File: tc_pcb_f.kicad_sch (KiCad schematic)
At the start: 7 parts, among them U1 32u4, U2 MAX31855, U3 MAX31855, U4 MAX31855, U5 MAX31855, U6 MAX31855, U7 extPWR

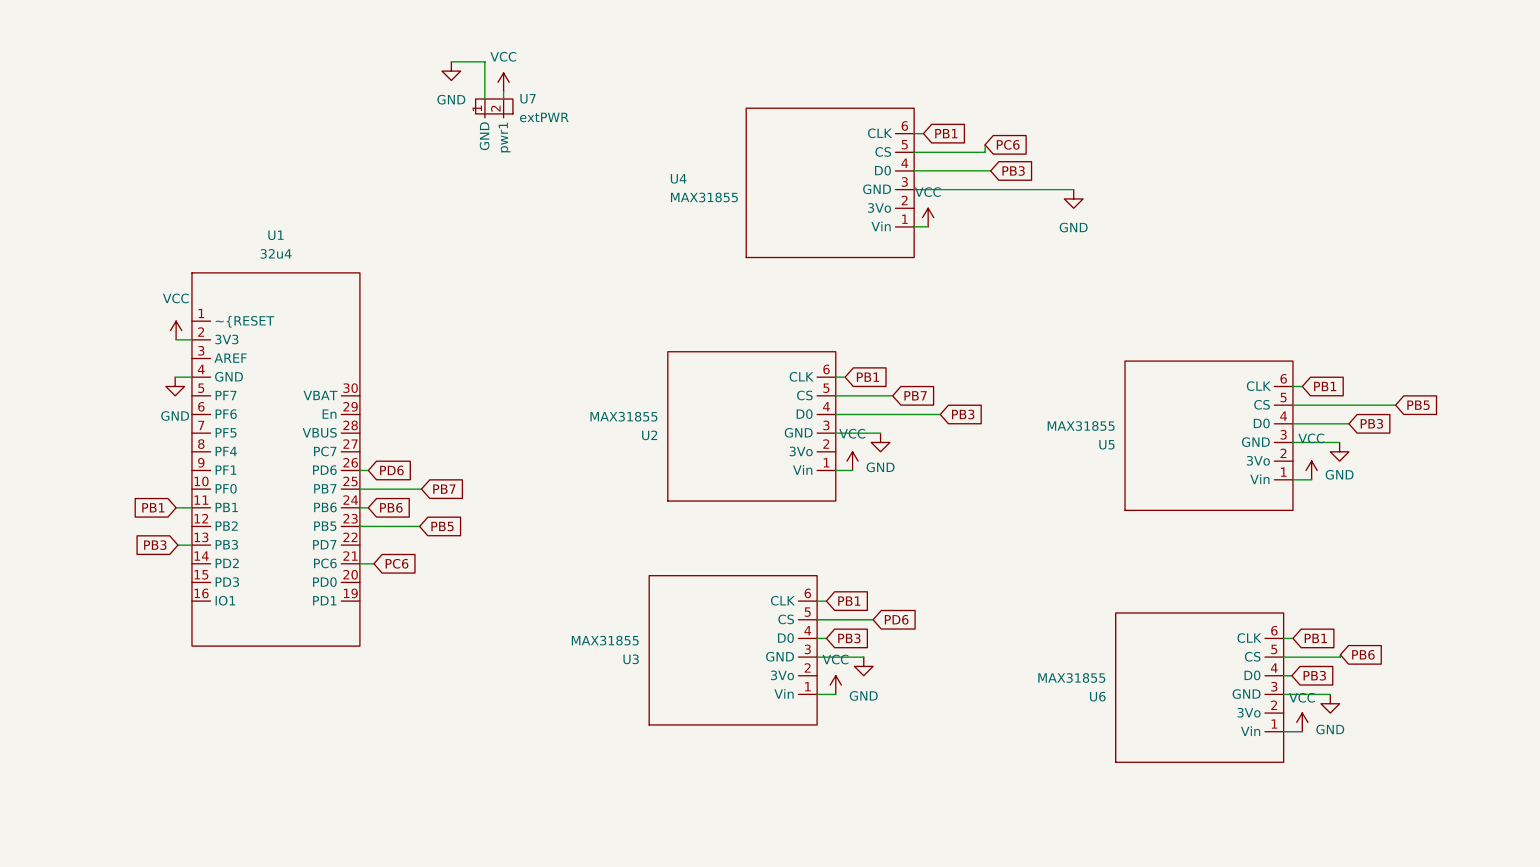
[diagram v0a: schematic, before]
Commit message: finished layout for 8 sensor board
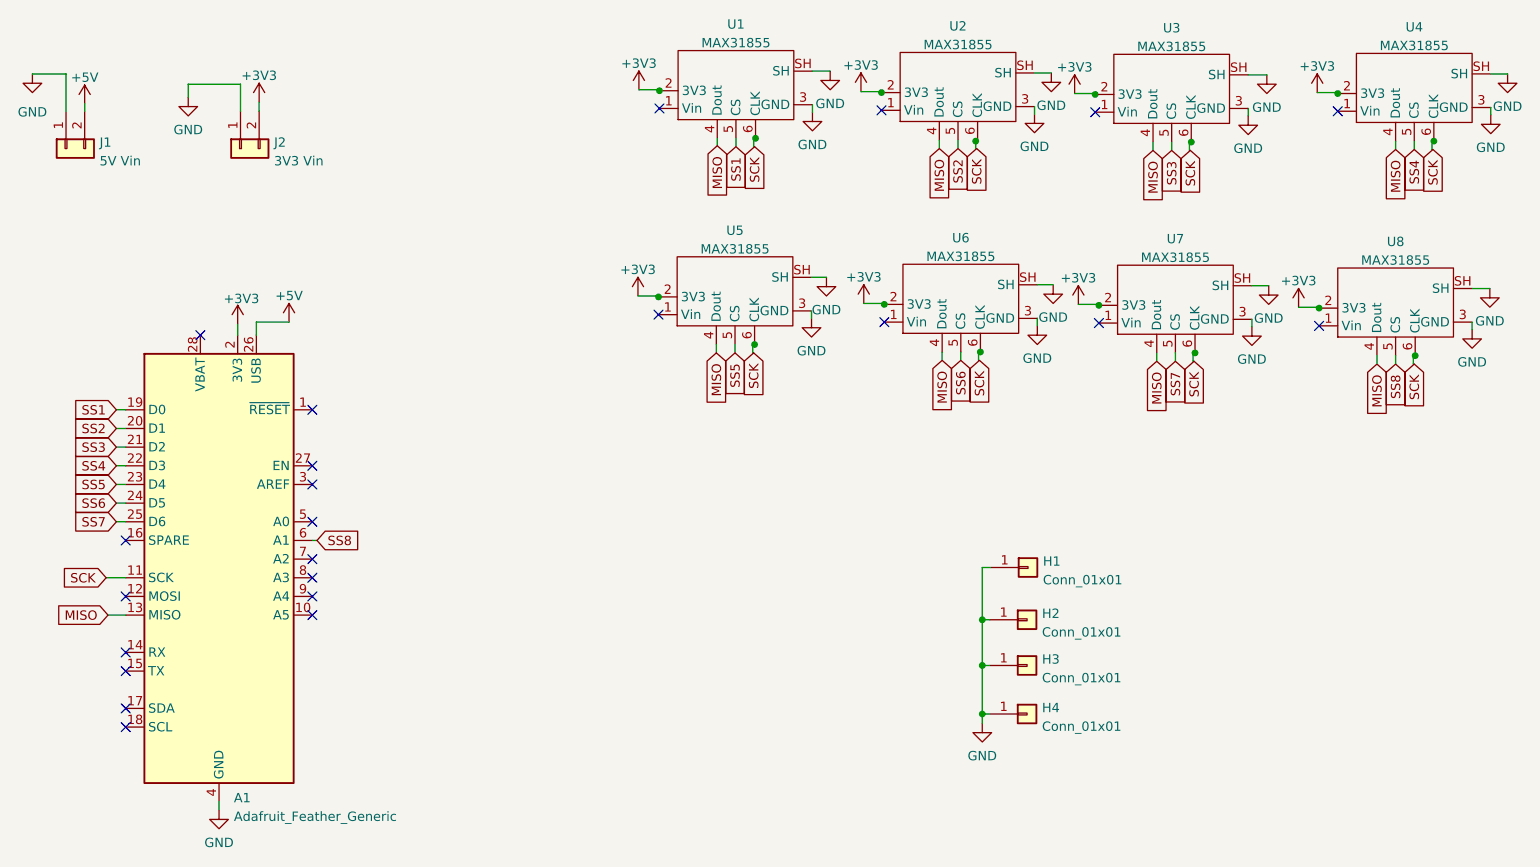
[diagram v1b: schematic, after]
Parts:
- removed U1: 32u4, thermo:32u4, symbol New_Library_0:32u4
- removed U2, U3, U4, U5, U6: MAX31855, thermo:MAX31855, symbol New_Library_0:MAX31855
- removed U7: extPWR, thermo:extPWR, symbol New_Library_0:extPWR
- added A1: Adafruit_Feather_Generic, mcu:Adafruit_Feather, symbol MCU_Module:Adafruit_Feather_Generic
- added H1, H2, H3, H4: Conn_01x01, mounting_holes:3mm_hole, symbol Connector_Generic:Conn_01x01
- added J1: 5V Vin, dupont_connectors:dupont2x1, symbol Connector_Generic:Conn_01x02
- added J2: 3V3 Vin, dupont_connectors:dupont2x1, symbol Connector_Generic:Conn_01x02
- added U1, U2, U3, U4, U5, U6, U7, U8: MAX31855, max:adafruit_max31855, symbol max31855:MAX31855
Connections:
- net GND: now also A1.4 (GND), H1.1 (Pin_1), H2.1 (Pin_1), H3.1 (Pin_1), H4.1 (Pin_1), J1.1 (Pin_1), J2.1 (Pin_1), U1.3 (GND), U1.SH, U2.3 (GND), U2.SH, U3.3 (GND), U3.SH, U4.3 (GND), U4.SH, U5.3 (GND), U5.SH, U6.3 (GND), U6.SH, U7.3 (GND), U7.SH, U8.3 (GND), U8.SH
- new net +3V3: A1.2 (3V3), J2.2 (Pin_2), U1.2 (3V3), U2.2 (3V3), U3.2 (3V3), U4.2 (3V3), U5.2 (3V3), U6.2 (3V3), U7.2 (3V3), U8.2 (3V3)
- new net +5V: A1.26 (USB), J1.2 (Pin_2)
- new net MISO: A1.13 (MISO), U1.4 (Dout), U2.4 (Dout), U3.4 (Dout), U4.4 (Dout), U5.4 (Dout), U6.4 (Dout), U7.4 (Dout), U8.4 (Dout)
- new net SCK: A1.11 (SCK), U1.6 (CLK), U2.6 (CLK), U3.6 (CLK), U4.6 (CLK), U5.6 (CLK), U6.6 (CLK), U7.6 (CLK), U8.6 (CLK)
- new net SS1: A1.19 (D0), U1.5 (CS)
- new net SS2: A1.20 (D1), U2.5 (CS)
- new net SS3: A1.21 (D2), U3.5 (CS)
- new net SS4: A1.22 (D3), U4.5 (CS)
- new net SS5: A1.23 (D4), U5.5 (CS)
- new net SS6: A1.24 (D5), U6.5 (CS)
- new net SS7: A1.25 (D6), U7.5 (CS)
- new net SS8: A1.6 (A1), U8.5 (CS)
- no-connect marks 0 -> 23
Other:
- title: (none) -> II-Lab 900MHz 8 Thermocouple Board
